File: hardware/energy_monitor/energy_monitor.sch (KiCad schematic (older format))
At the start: 139 parts, among them J1 Screw_Terminal_01x03, J2 Screw_Terminal_01x04, J3 Screw_Terminal_01x04, J4 Screw_Terminal_01x04, J5 USB_OTG, Q1 MMBT2222, Q2 MMBT2222, U1 RAC04, U2 TPS730, U3 TPS723, U4 ADS131E08, U5 AP2112, U6 CP2104, U7 ESP-WROOM-32U, U8 ISO7421, U9 ISO7420

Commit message: Working on layout
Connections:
- no-connect marks 1 -> 10
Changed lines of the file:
@@
 	16000 2200 16000 2150
 Connection ~ 16000 2150
+NoConn ~ 9100 8100
+NoConn ~ 9100 8000
+NoConn ~ 9100 7900
+NoConn ~ 9100 7700
+NoConn ~ 9100 7600
+NoConn ~ 11300 7100
+NoConn ~ 11300 7200
+NoConn ~ 11300 7300
+NoConn ~ 11300 7400
 $EndSCHEMATC

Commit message: Working on layout
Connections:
- net labels added: ADC_DRDY, ADC_PWDN, ADC_RESET, ADC_START
- net labels removed: DRDY, PWDN, START
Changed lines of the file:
@@
 CS
 Text Label 11500 5600 0    60   ~ 0
-START
+ADC_START
 Text Label 11500 5700 0    60   ~ 0
-DRDY
-Text Label 15850 6800 0    60   ~ 0
-START
-Text Label 15850 6900 0    60   ~ 0
-DRDY
+ADC_DRDY
 Text Label 15350 6050 0    60   ~ 0
 CS
@@
 MISO
 Text Label 11500 4900 0    60   ~ 0
-RESET
+ADC_RESET
 Text Label 11500 5000 0    60   ~ 0
-PWDN
-Text Label 15850 6600 0    60   ~ 0
-RESET
-Text Label 15850 6700 0    60   ~ 0
-PWDN
+ADC_PWDN
 $Comp
 L +3.3V #PWR91
@@
 	11400 8100 11300 8100
 Wire Wire Line
-	11400 5400 11400 8200
-Wire Wire Line
 	8750 7400 9100 7400
 Wire Wire Line
@@
 	11400 5400 11300 5400
 Connection ~ 11400 8100
-Wire Wire Line
-	11900 5600 11300 5600
-Wire Wire Line
-	11900 5700 11300 5700
-Wire Wire Line
-	11900 5900 11300 5900
-Wire Wire Line
-	11900 6000 11300 6000
-Wire Wire Line
-	11900 6100 11300 6100
-Wire Wire Line
-	11900 6200 11300 6200
-Wire Wire Line
-	11900 5000 11300 5000
-Wire Wire Line
-	11900 4900 11300 4900
 Wire Wire Line
 	11300 5200 11400 5200
@@
 NoConn ~ 11300 7300
 NoConn ~ 11300 7400
+Text Label 15700 6850 0    60   ~ 0
+ADC_RESET
+Text Label 15700 7050 0    60   ~ 0
+ADC_PWDN
+Text Label 15650 7200 0    60   ~ 0
+ADC_START
+Text Label 15700 7350 0    60   ~ 0
+ADC_DRDY
+Wire Wire Line
+	12000 4900 11300 4900
+Wire Wire Line
+	12000 5000 11300 5000
+Wire Wire Line
+	11400 5400 11400 8200
+Wire Wire Line
+	12000 5600 11300 5600
+Wire Wire Line
+	12000 5700 11300 5700
+Wire Wire Line
+	12000 5900 11300 5900
+Wire Wire Line
+	12000 6000 11300 6000
+Wire Wire Line
+	12000 6100 11300 6100
+Wire Wire Line
+	12000 6200 11300 6200
 $EndSCHEMATC

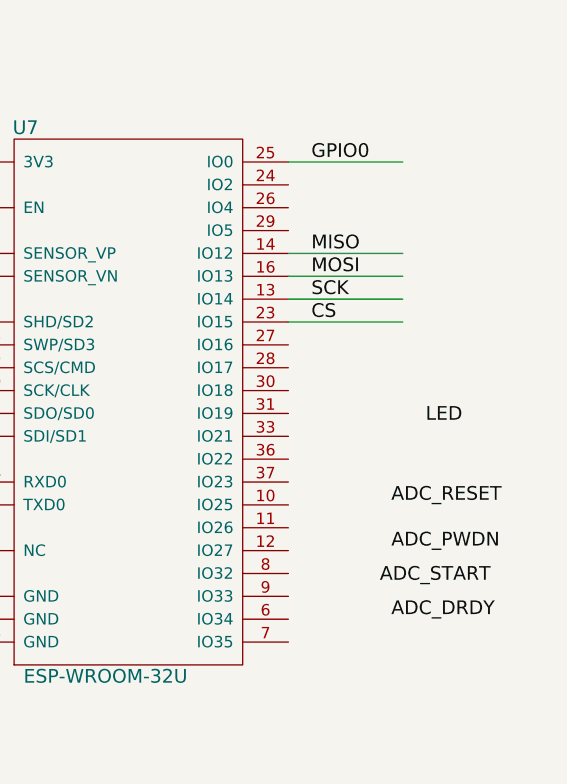
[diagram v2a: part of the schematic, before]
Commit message: Finished routing board
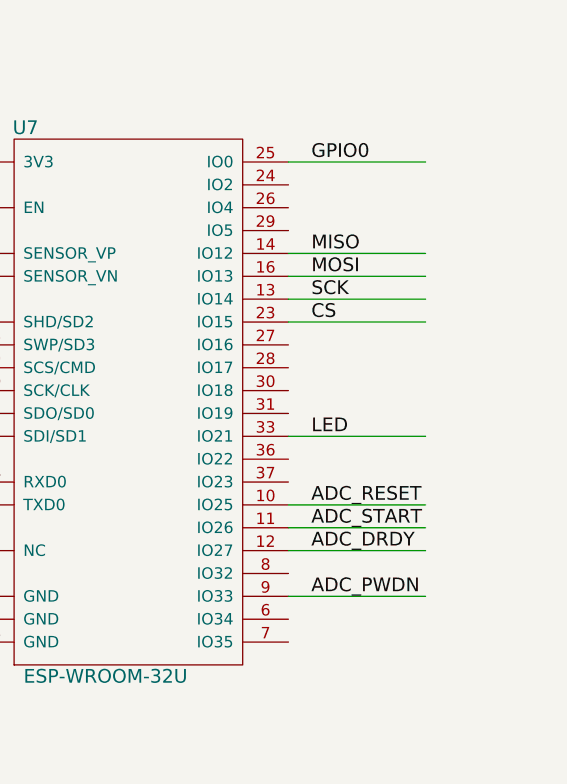
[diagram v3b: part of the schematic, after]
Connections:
- wire segments 490 -> 495

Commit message: Added 2 more LEDs.  Added labels to LEDs.  Added board rev #
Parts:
- added D25, D26: GRN, Diodes_SMD:D_0603, symbol LED
- added R33, R34: 1k, Resistors_SMD:R_0603, symbol R
- F1, F2: value 1A/300V -> 1A/250V
- renumbered D25 to D27, D26 to D28, R33 to R35, R34 to R36, R35 to R37, R36 to R38, R37 to R39
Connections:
- net labels added: LED1, LED2, LED3
- net labels removed: LED
- wire segments 495 -> 503
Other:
- moved on the sheet: D23, D24, Q1, Q2, R31, R32, R35, R36
